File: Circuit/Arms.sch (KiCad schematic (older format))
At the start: 6 parts, among them P10 LW_ADC, P11 RU_ADC, P12 RV_ADC, P13 RW_ADC, P8 LU_ADC, P9 LV_ADC

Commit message: 実態配線図書き始め
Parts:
- P10, P11, P12, P13, P8, P9: footprint (none) -> YASU:XA_3Pin
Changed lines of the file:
@@
 LIBS:contrib
 LIBS:valves
+LIBS:YASU
 LIBS:device
+LIBS:robocon_sch
 LIBS:rhand_controller-cache
 EELAYER 25 0
@@
 F 0 "P12" H 4850 4650 50  0000 C CNN
 F 1 "RV_ADC" V 4950 4450 50  0000 C CNN
-F 2 "" H 4850 4450 50  0001 C CNN
+F 2 "YASU:XA_3Pin" H 4850 4450 50  0001 C CNN
 F 3 "" H 4850 4450 50  0000 C CNN
 	1    4850 4450
@@
 F 0 "P13" H 4850 5400 50  0000 C CNN
 F 1 "RW_ADC" V 4950 5200 50  0000 C CNN
-F 2 "" H 4850 5200 50  0001 C CNN
+F 2 "YASU:XA_3Pin" H 4850 5200 50  0001 C CNN
 F 3 "" H 4850 5200 50  0000 C CNN
 	1    4850 5200
@@
 F 0 "P11" H 4850 3900 50  0000 C CNN
 F 1 "RU_ADC" V 4950 3700 50  0000 C CNN
-F 2 "" H 4850 3700 50  0001 C CNN
+F 2 "YASU:XA_3Pin" H 4850 3700 50  0001 C CNN
 F 3 "" H 4850 3700 50  0000 C CNN
 	1    4850 3700
@@
 F 0 "P9" H 3600 4650 50  0000 C CNN
 F 1 "LV_ADC" V 3700 4450 50  0000 C CNN
-F 2 "" H 3600 4450 50  0001 C CNN
+F 2 "YASU:XA_3Pin" H 3600 4450 50  0001 C CNN
 F 3 "" H 3600 4450 50  0000 C CNN
 	1    3600 4450
@@
 F 0 "P10" H 3600 5400 50  0000 C CNN
 F 1 "LW_ADC" V 3700 5200 50  0000 C CNN
-F 2 "" H 3600 5200 50  0001 C CNN
+F 2 "YASU:XA_3Pin" H 3600 5200 50  0001 C CNN
 F 3 "" H 3600 5200 50  0000 C CNN
 	1    3600 5200
@@
 F 0 "P8" H 3600 3900 50  0000 C CNN
 F 1 "LU_ADC" V 3700 3700 50  0000 C CNN
-F 2 "" H 3600 3700 50  0001 C CNN
+F 2 "YASU:XA_3Pin" H 3600 3700 50  0001 C CNN
 F 3 "" H 3600 3700 50  0000 C CNN
 	1    3600 3700

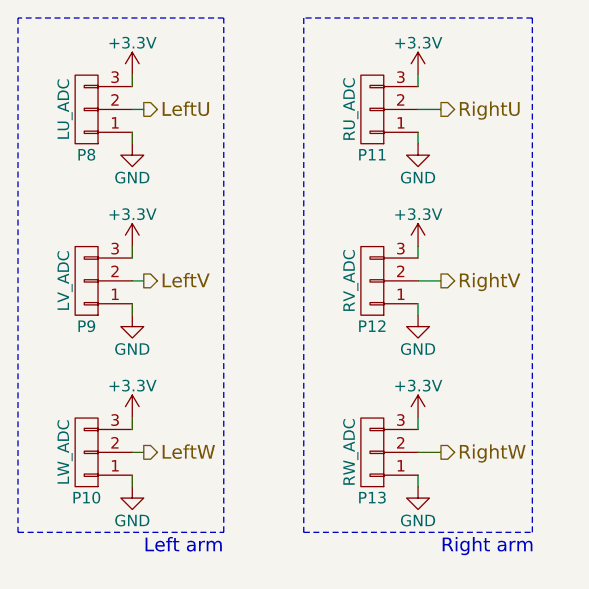
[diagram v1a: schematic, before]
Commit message: 部品割り付けの完了
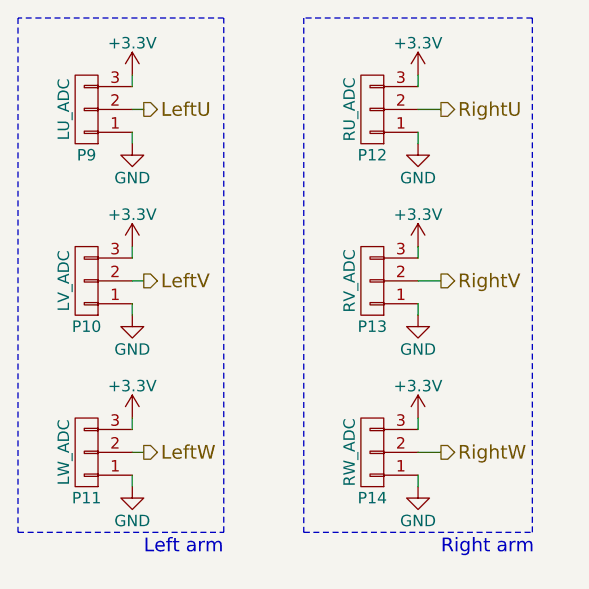
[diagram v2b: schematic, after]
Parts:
- renumbered P9 to P10, P10 to P11, P11 to P12, P12 to P13, P13 to P14, P8 to P9
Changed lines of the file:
@@
 LIBS:YASU
 LIBS:device
-LIBS:robocon_sch
 LIBS:rhand_controller-cache
 EELAYER 25 0
@@
 $EndDescr
 $Comp
-L CONN_01X03 P12
+L CONN_01X03 P13
 U 1 1 593EB2B2
 P 4850 4450
-F 0 "P12" H 4850 4650 50  0000 C CNN
+F 0 "P13" H 4850 4650 50  0000 C CNN
 F 1 "RV_ADC" V 4950 4450 50  0000 C CNN
 F 2 "YASU:XA_3Pin" H 4850 4450 50  0001 C CNN
@@
 $EndComp
 $Comp
-L CONN_01X03 P13
+L CONN_01X03 P14
 U 1 1 593EB2B9
 P 4850 5200
-F 0 "P13" H 4850 5400 50  0000 C CNN
+F 0 "P14" H 4850 5400 50  0000 C CNN
 F 1 "RW_ADC" V 4950 5200 50  0000 C CNN
 F 2 "YASU:XA_3Pin" H 4850 5200 50  0001 C CNN
@@
 $EndComp
 $Comp
-L CONN_01X03 P11
+L CONN_01X03 P12
 U 1 1 593EB2C0
 P 4850 3700
-F 0 "P11" H 4850 3900 50  0000 C CNN
+F 0 "P12" H 4850 3900 50  0000 C CNN
 F 1 "RU_ADC" V 4950 3700 50  0000 C CNN
 F 2 "YASU:XA_3Pin" H 4850 3700 50  0001 C CNN
@@
 $EndComp
 $Comp
-L CONN_01X03 P9
+L CONN_01X03 P10
 U 1 1 593EB2EE
 P 3600 4450
-F 0 "P9" H 3600 4650 50  0000 C CNN
+F 0 "P10" H 3600 4650 50  0000 C CNN
 F 1 "LV_ADC" V 3700 4450 50  0000 C CNN
 F 2 "YASU:XA_3Pin" H 3600 4450 50  0001 C CNN
@@
 $EndComp
 $Comp
-L CONN_01X03 P10
+L CONN_01X03 P11
 U 1 1 593EB2F5
 P 3600 5200
-F 0 "P10" H 3600 5400 50  0000 C CNN
+F 0 "P11" H 3600 5400 50  0000 C CNN
 F 1 "LW_ADC" V 3700 5200 50  0000 C CNN
 F 2 "YASU:XA_3Pin" H 3600 5200 50  0001 C CNN
@@
 $EndComp
 $Comp
-L CONN_01X03 P8
+L CONN_01X03 P9
 U 1 1 593EB2FC
 P 3600 3700
-F 0 "P8" H 3600 3900 50  0000 C CNN
+F 0 "P9" H 3600 3900 50  0000 C CNN
 F 1 "LU_ADC" V 3700 3700 50  0000 C CNN
 F 2 "YASU:XA_3Pin" H 3600 3700 50  0001 C CNN

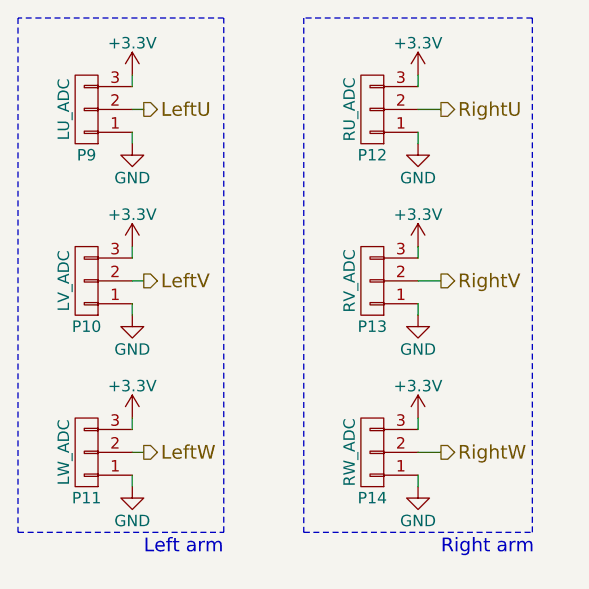
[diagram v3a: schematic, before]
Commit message: ADCのピン配置修正と配線引きはじめ
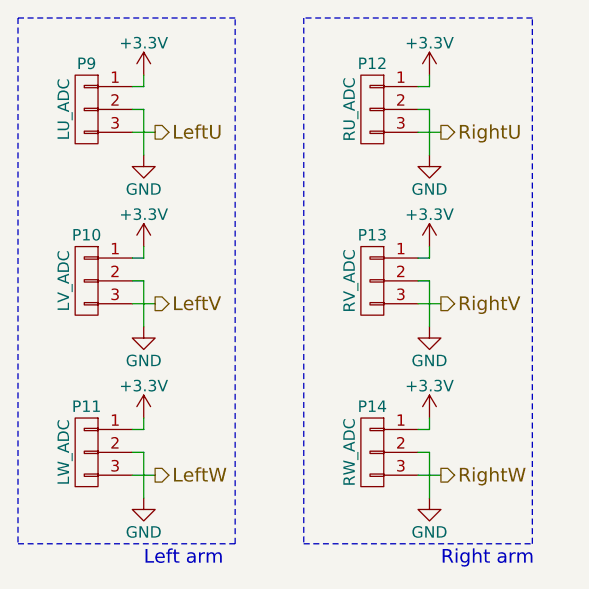
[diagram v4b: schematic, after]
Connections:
- net +3V3: now also P10.1 (P1), P11.1 (P1), P12.1 (P1), P13.1 (P1), P14.1 (P1), P9.1 (P1); no longer P10.3 (P3), P11.3 (P3), P12.3 (P3), P13.3 (P3), P14.3 (P3), P9.3 (P3)
- net GND: now also P10.2 (P2), P11.2 (P2), P12.2 (P2), P13.2 (P2), P14.2 (P2), P9.2 (P2); no longer P10.1 (P1), P11.1 (P1), P12.1 (P1), P13.1 (P1), P14.1 (P1), P9.1 (P1)
- net LeftU: now also P9.3 (P3); no longer P9.2 (P2)
- net LeftV: now also P10.3 (P3); no longer P10.2 (P2)
- net LeftW: now also P11.3 (P3); no longer P11.2 (P2)
- net RightU: now also P12.3 (P3); no longer P12.2 (P2)
- net RightV: now also P13.3 (P3); no longer P13.2 (P2)
- net RightW: now also P14.3 (P3); no longer P14.2 (P2)
